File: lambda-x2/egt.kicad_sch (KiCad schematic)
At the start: 9 parts, among them U1 MAX31855KASA

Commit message: more progress
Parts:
- added C58, C60: 10nF 50V, Capacitor_SMD:C_0402_1005Metric, symbol Device:C
- added C59, C61, C62: 100n, Capacitor_SMD:C_0402_1005Metric, symbol Device:C
- added R92, R93: (no value), symbol Device:R
- added U15: (no value), symbol Sensor_Temperature:MAX31856
- C48, C50: value (none) -> 10nF 50V; footprint (none) -> Capacitor_SMD:C_0402_1005Metric
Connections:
- net GND: now also C58.2, C60.2, C61.2, C62.2, U15.1 (AGND), U15.14 (DGND)
- net SPI_CS: now also U15.9 (~{CS})
- net SPI_SCK: now also U15.10 (SCK)
- net SPI_SO: now also U15.11 (SDO)
- net Vcc: now also C61.1, C62.1, U15.5 (AVDD), U15.8 (DVDD)
- net at C49.2, C50.1, D7.1 (K)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: now also R92.1
- net at C48.1, C49.1, D7.2 (K)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: now also R93.1, U15.2 (BIAS)
- new net: C58.1, C59.1, R93.2, U15.3 (T-)
- new net: C59.2, C60.1, R92.2, U15.4 (T+)
- new net SPI_SI: U15.12 (SDI)
- no-connect marks 0 -> 2
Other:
- note added: "Optional part: 10x time more expensive more features protected up to 45V on inputs"
- moved on the sheet: C37, C43, D7, L1, L3

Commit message: Progress
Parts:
- R92, R93: value (none) -> 100R; footprint (none) -> Resistor_SMD:R_0402_1005Metric
- U15: value (none) -> MAX31856; footprint (none) -> Package_SO:TSSOP-14_4.4x5mm_P0.65mm
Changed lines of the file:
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@@
     (in_bom yes) (on_board yes)
     (property "Reference" "R92" (id 0) (at 44.45 96.52 90))
-    (property "Value" "" (id 1) (at 44.45 99.06 90))
-    (property "Footprint" "" (id 2) (at 44.45 99.822 90)
+    (property "Value" "100R" (id 1) (at 44.45 99.06 90))
+    (property "Footprint" "Resistor_SMD:R_0402_1005Metric" (id 2) (at 44.45 99.822 90)
       (effects (font (size 1.27 1.27)) hide)
     )
@@
     (in_bom yes) (on_board yes)
     (property "Reference" "R93" (id 0) (at 44.45 106.68 90))
-    (property "Value" "" (id 1) (at 44.45 109.22 90))
-    (property "Footprint" "" (id 2) (at 44.45 102.362 90)
+    (property "Value" "100R" (id 1) (at 44.45 109.22 90))
+    (property "Footprint" "Resistor_SMD:R_0402_1005Metric" (id 2) (at 44.45 102.362 90)
       (effects (font (size 1.27 1.27)) hide)
     )
@@
       (effects (font (size 1.27 1.27)) (justify left))
     )
-    (property "Value" "" (id 1) (at 83.2994 88.9 0)
-      (effects (font (size 1.27 1.27)) (justify left))
-    )
-    (property "Footprint" "" (id 2) (at 82.55 118.11 0)
+    (property "Value" "MAX31856" (id 1) (at 83.2994 88.9 0)
+      (effects (font (size 1.27 1.27)) (justify left))
+    )
+    (property "Footprint" "Package_SO:TSSOP-14_4.4x5mm_P0.65mm" (id 2) (at 82.55 118.11 0)
       (effects (font (size 1.27 1.27)) (justify left) hide)
     )

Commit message: Progress
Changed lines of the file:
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@@
+    (stroke (width 0) (type default) (color 0 0 0 0))
+  )
+  (wire (pts (xy 33.02 121.92) (xy 33.02 120.65))
     (stroke (width 0) (type default) (color 0 0 0 0))
   )
@@
     (stroke (width 0) (type default) (color 0 0 0 0))
   )
-  (wire (pts (xy 63.5 116.84) (xy 63.5 119.38))
+  (wire (pts (xy 63.5 116.84) (xy 63.5 121.92))
     (stroke (width 0) (type default) (color 0 0 0 0))
   )
@@
     (stroke (width 0) (type default) (color 0 0 0 0))
   )
-  (wire (pts (xy 52.07 116.84) (xy 52.07 119.38))
+  (wire (pts (xy 52.07 116.84) (xy 52.07 121.92))
     (stroke (width 0) (type default) (color 0 0 0 0))
   )
@@
     (pin "2")
   )
-  (symbol (lib_id "power:GND") (at 106.68 85.09 0) (unit 1)
+  (symbol (lib_name "GND_1") (lib_id "power:GND") (at 106.68 85.09 0) (unit 1)
     (in_bom yes) (on_board yes)
     (property "Reference" "#PWR0173" (id 0) (at 106.68 91.44 0)
       (effects (font (size 1.27 1.27)) hide)
     )
-    (property "Value" "GND" (id 1) (at 106.807 89.4842 0))
+    (property "Value" "" (id 1) (at 106.807 89.4842 0)
+      (effects (font (size 1.27 1.27)) hide)
+    )
     (property "Footprint" "" (id 2) (at 106.68 85.09 0)
       (effects (font (size 1.27 1.27)) hide)
@@
     (pin "2")
   )
-  (symbol (lib_id "power:GND") (at 90.17 29.21 0) (unit 1)
+  (symbol (lib_name "GND_4") (lib_id "power:GND") (at 90.17 29.21 0) (unit 1)
     (in_bom yes) (on_board yes)
     (property "Reference" "#PWR0150" (id 0) (at 90.17 35.56 0)
       (effects (font (size 1.27 1.27)) hide)
     )
-    (property "Value" "GND" (id 1) (at 90.297 33.6042 0))
+    (property "Value" "" (id 1) (at 90.297 33.6042 0)
+      (effects (font (size 1.27 1.27)) hide)
+    )
     (property "Footprint" "" (id 2) (at 90.17 29.21 0)
       (effects (font (size 1.27 1.27)) hide)
@@
     (pin "2")
   )
-  (symbol (lib_id "power:GND") (at 52.07 119.38 0) (unit 1)
-    (in_bom yes) (on_board yes)
-    (property "Reference" "#PWR0172" (id 0) (at 52.07 125.73 0)
-      (effects (font (size 1.27 1.27)) hide)
-    )
-    (property "Value" "GND" (id 1) (at 52.197 123.7742 0))
-    (property "Footprint" "" (id 2) (at 52.07 119.38 0)
-      (effects (font (size 1.27 1.27)) hide)
-    )
-    (property "Datasheet" "" (id 3) (at 52.07 119.38 0)
-      (effects (font (size 1.27 1.27)) hide)
-    )
-    (pin "1")
-  )
-  (symbol (lib_id "power:GND") (at 76.2 121.92 0) (unit 1)
+  (symbol (lib_name "GND_8") (lib_id "power:GND") (at 52.07 121.92 0) (unit 1)
+    (in_bom yes) (on_board yes)
+    (property "Reference" "#PWR0172" (id 0) (at 52.07 128.27 0)
+      (effects (font (size 1.27 1.27)) hide)
+    )
+    (property "Value" "" (id 1) (at 52.197 126.3142 0)
+      (effects (font (size 1.27 1.27)) hide)
+    )
+    (property "Footprint" "" (id 2) (at 52.07 121.92 0)
+      (effects (font (size 1.27 1.27)) hide)
+    )
+    (property "Datasheet" "" (id 3) (at 52.07 121.92 0)
+      (effects (font (size 1.27 1.27)) hide)
+    )
+    (pin "1")
+  )
+  (symbol (lib_name "GND_10") (lib_id "power:GND") (at 76.2 121.92 0) (unit 1)
     (in_bom yes) (on_board yes)
     (property "Reference" "#PWR0175" (id 0) (at 76.2 128.27 0)
       (effects (font (size 1.27 1.27)) hide)
     )
-    (property "Value" "GND" (id 1) (at 76.327 126.3142 0))
+    (property "Value" "" (id 1) (at 76.327 126.3142 0)
+      (effects (font (size 1.27 1.27)) hide)
+    )
     (property "Footprint" "" (id 2) (at 76.2 121.92 0)
       (effects (font (size 1.27 1.27)) hide)
@@
     (pin "1")
   )
-  (symbol (lib_id "power:GND") (at 81.28 121.92 0) (unit 1)
+  (symbol (lib_name "GND_11") (lib_id "power:GND") (at 81.28 121.92 0) (unit 1)
     (in_bom yes) (on_board yes)
     (property "Reference" "#PWR0176" (id 0) (at 81.28 128.27 0)
       (effects (font (size 1.27 1.27)) hide)
     )
-    (property "Value" "GND" (id 1) (at 81.407 126.3142 0))
+    (property "Value" "" (id 1) (at 81.407 126.3142 0)
+      (effects (font (size 1.27 1.27)) hide)
+    )
     (property "Footprint" "" (id 2) (at 81.28 121.92 0)
       (effects (font (size 1.27 1.27)) hide)
@@
     (pin "9")
   )
-  (symbol (lib_id "power:GND") (at 128.27 29.21 0) (unit 1)
+  (symbol (lib_name "GND_3") (lib_id "power:GND") (at 128.27 29.21 0) (unit 1)
     (in_bom yes) (on_board yes)
     (property "Reference" "#PWR0149" (id 0) (at 128.27 35.56 0)
       (effects (font (size 1.27 1.27)) hide)
     )
-    (property "Value" "GND" (id 1) (at 128.397 33.6042 0))
+    (property "Value" "" (id 1) (at 128.397 33.6042 0)
+      (effects (font (size 1.27 1.27)) hide)
+    )
     (property "Footprint" "" (id 2) (at 128.27 29.21 0)
       (effects (font (size 1.27 1.27)) hide)
@@
     (pin "1")
   )
-  (symbol (lib_id "power:GND") (at 53.34 59.69 0) (unit 1)
+  (symbol (lib_name "GND_5") (lib_id "power:GND") (at 53.34 59.69 0) (unit 1)
     (in_bom yes) (on_board yes)
     (property "Reference" "#PWR0156" (id 0) (at 53.34 66.04 0)
       (effects (font (size 1.27 1.27)) hide)
     )
-    (property "Value" "GND" (id 1) (at 53.467 64.0842 0))
+    (property "Value" "" (id 1) (at 53.467 64.0842 0)
+      (effects (font (size 1.27 1.27)) hide)
+    )
     (property "Footprint" "" (id 2) (at 53.34 59.69 0)
       (effects (font (size 1.27 1.27)) hide)
@@
     (pin "1")
   )
-  (symbol (lib_id "power:GND") (at 66.04 59.69 0) (unit 1)
+  (symbol (lib_name "GND_6") (lib_id "power:GND") (at 66.04 59.69 0) (unit 1)
     (in_bom yes) (on_board yes)
     (property "Reference" "#PWR0157" (id 0) (at 66.04 66.04 0)
       (effects (font (size 1.27 1.27)) hide)
     )
-    (property "Value" "GND" (id 1) (at 66.167 64.0842 0))
+    (property "Value" "" (id 1) (at 66.167 64.0842 0)
+      (effects (font (size 1.27 1.27)) hide)
+    )
     (property "Footprint" "" (id 2) (at 66.04 59.69 0)
       (effects (font (size 1.27 1.27)) hide)
@@
     (pin "1")
   )
-  (symbol (lib_id "power:GND") (at 80.01 57.15 0) (unit 1)
+  (symbol (lib_name "GND_7") (lib_id "power:GND") (at 80.01 57.15 0) (unit 1)
     (in_bom yes) (on_board yes)
     (property "Reference" "#PWR0148" (id 0) (at 80.01 63.5 0)
       (effects (font (size 1.27 1.27)) hide)
     )
-    (property "Value" "GND" (id 1) (at 80.137 61.5442 0))
+    (property "Value" "" (id 1) (at 80.137 61.5442 0)
+      (effects (font (size 1.27 1.27)) hide)
+    )
     (property "Footprint" "" (id 2) (at 80.01 57.15 0)
       (effects (font (size 1.27 1.27)) hide)
@@
     (pin "2")
   )
-  (symbol (lib_id "power:GND") (at 116.84 85.09 0) (unit 1)
+  (symbol (lib_name "GND_2") (lib_id "power:GND") (at 116.84 85.09 0) (unit 1)
     (in_bom yes) (on_board yes)
     (property "Reference" "#PWR0174" (id 0) (at 116.84 91.44 0)
       (effects (font (size 1.27 1.27)) hide)
     )
-    (property "Value" "GND" (id 1) (at 116.967 89.4842 0))
+    (property "Value" "" (id 1) (at 116.967 89.4842 0)
+      (effects (font (size 1.27 1.27)) hide)
+    )
     (property "Footprint" "" (id 2) (at 116.84 85.09 0)
       (effects (font (size 1.27 1.27)) hide)
@@
     (pin "2")
   )
-  (symbol (lib_id "power:GND") (at 63.5 119.38 0) (unit 1)
-    (in_bom yes) (on_board yes)
-    (property "Reference" "#PWR0177" (id 0) (at 63.5 125.73 0)
-      (effects (font (size 1.27 1.27)) hide)
-    )
-    (property "Value" "GND" (id 1) (at 63.627 123.7742 0))
-    (property "Footprint" "" (id 2) (at 63.5 119.38 0)
-      (effects (font (size 1.27 1.27)) hide)
-    )
-    (property "Datasheet" "" (id 3) (at 63.5 119.38 0)
-      (effects (font (size 1.27 1.27)) hide)
-    )
-    (pin "1")
-  )
-  (symbol (lib_id "power:GND") (at 33.02 120.65 0) (unit 1)
-    (in_bom yes) (on_board yes)
-    (property "Reference" "#PWR0154" (id 0) (at 33.02 127 0)
-      (effects (font (size 1.27 1.27)) hide)
-    )
-    (property "Value" "GND" (id 1) (at 33.147 125.0442 0))
-    (property "Footprint" "" (id 2) (at 33.02 120.65 0)
-      (effects (font (size 1.27 1.27)) hide)
-    )
-    (property "Datasheet" "" (id 3) (at 33.02 120.65 0)
-      (effects (font (size 1.27 1.27)) hide)
-    )
+  (symbol (lib_name "GND_9") (lib_id "power:GND") (at 63.5 121.92 0) (unit 1)
+    (in_bom yes) (on_board yes)
+    (property "Reference" "#PWR0177" (id 0) (at 63.5 128.27 0)
+      (effects (font (size 1.27 1.27)) hide)
+    )
+    (property "Value" "" (id 1) (at 63.627 126.3142 0)
+      (effects (font (size 1.27 1.27)) hide)
+    )
+    (property "Footprint" "" (id 2) (at 63.5 121.92 0)
+      (effects (font (size 1.27 1.27)) hide)
+    )
+    (property "Datasheet" "" (id 3) (at 63.5 121.92 0)
+      (effects (font (size 1.27 1.27)) hide)
+    )
+    (pin "1")
+  )
+  (symbol (lib_id "power:GND") (at 33.02 121.92 0) (unit 1)
+    (in_bom yes) (on_board yes)
+    (property "Reference" "#PWR0154" (id 0) (at 33.02 128.27 0)
+      (effects (font (size 1.27 1.27)) hide)
+    )
+    (property "Value" "" (id 1) (at 33.147 126.3142 0)
+      (effects (font (size 1.27 1.27)) hide)
+    )
+    (property "Footprint" "" (id 2) (at 33.02 121.92 0)
+      (effects (font (size 1.27 1.27)) hide)
+    )
+    (property "Datasheet" "" (id 3) (at 33.02 121.92 0)
+      (effects (font (size 1.27 1.27)) hide)
+    )

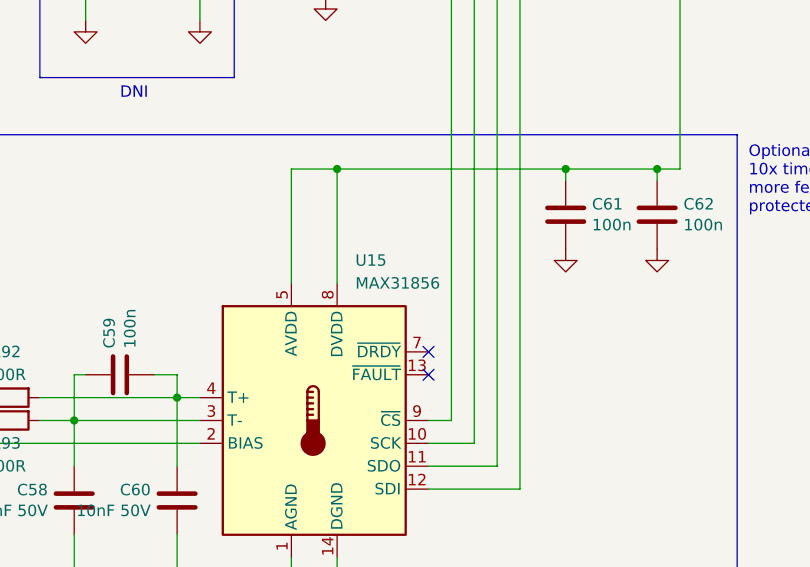
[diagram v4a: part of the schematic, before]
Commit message: Remove MAX31856 from BOM
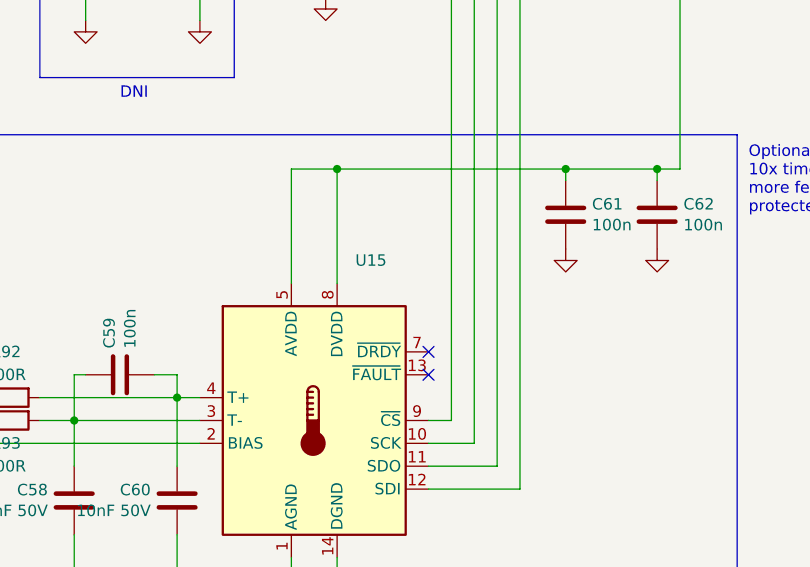
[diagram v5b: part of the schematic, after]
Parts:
- U15: value MAX31856 -> (none); footprint Package_SO:TSSOP-14_4.4x5mm_P0.65mm -> (none); now left out of the parts list
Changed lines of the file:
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@@
   )
   (symbol (lib_id "Sensor_Temperature:MAX31856") (at 78.74 104.14 0) (unit 1)
-    (in_bom yes) (on_board yes) (fields_autoplaced)
+    (in_bom no) (on_board yes) (fields_autoplaced)
     (property "Reference" "U15" (id 0) (at 83.2994 86.36 0)
       (effects (font (size 1.27 1.27)) (justify left))
     )
-    (property "Value" "MAX31856" (id 1) (at 83.2994 88.9 0)
+    (property "Value" "" (id 1) (at 83.2994 88.9 0)
       (effects (font (size 1.27 1.27)) (justify left))
     )
-    (property "Footprint" "Package_SO:TSSOP-14_4.4x5mm_P0.65mm" (id 2) (at 82.55 118.11 0)
+    (property "Footprint" "" (id 2) (at 82.55 118.11 0)
       (effects (font (size 1.27 1.27)) (justify left) hide)
     )

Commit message: lambda-x2: revork aux outputs, remove useless protection in LSU
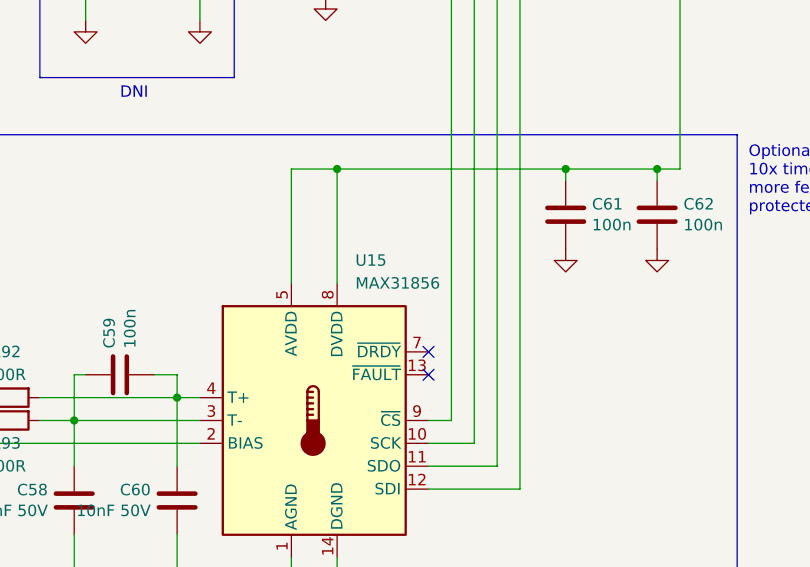
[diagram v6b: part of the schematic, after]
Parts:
- U15: value (none) -> MAX31856; footprint (none) -> Package_SO:TSSOP-14_4.4x5mm_P0.65mm
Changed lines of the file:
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@@
       (effects (font (size 1.27 1.27)) (justify left))
     )
-    (property "Value" "" (id 1) (at 83.2994 88.9 0)
+    (property "Value" "MAX31856" (id 1) (at 83.2994 88.9 0)
       (effects (font (size 1.27 1.27)) (justify left))
     )
-    (property "Footprint" "" (id 2) (at 82.55 118.11 0)
+    (property "Footprint" "Package_SO:TSSOP-14_4.4x5mm_P0.65mm" (id 2) (at 82.55 118.11 0)
       (effects (font (size 1.27 1.27)) (justify left) hide)
     )

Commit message: lambda-x2: final update, rev1
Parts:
- U1: value MAX31855KASA -> (none); footprint Package_SO:SOIC-8_3.9x4.9mm_P1.27mm -> (none); LCSC (none) -> C52028
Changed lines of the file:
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@@
       (effects (font (size 1.27 1.27)) (justify left))
     )
-    (property "Value" "MAX31855KASA" (id 1) (at 82.0294 34.29 0)
+    (property "Value" "" (id 1) (at 82.0294 34.29 0)
       (effects (font (size 1.27 1.27)) (justify left))
     )
-    (property "Footprint" "Package_SO:SOIC-8_3.9x4.9mm_P1.27mm" (id 2) (at 105.41 53.34 0)
+    (property "Footprint" "" (id 2) (at 105.41 53.34 0)
       (effects (font (size 1.27 1.27) italic) hide)
     )
@@
       (effects (font (size 1.27 1.27)) hide)
     )
+    (property "LCSC" "C52028" (id 4) (at 80.01 44.45 0)
+      (effects (font (size 1.27 1.27)) hide)
+    )

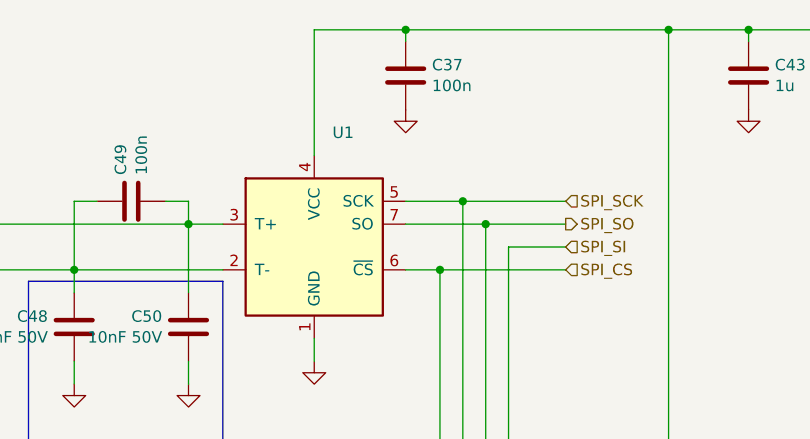
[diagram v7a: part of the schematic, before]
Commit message: lambda-x2: update BOM per JLC availability
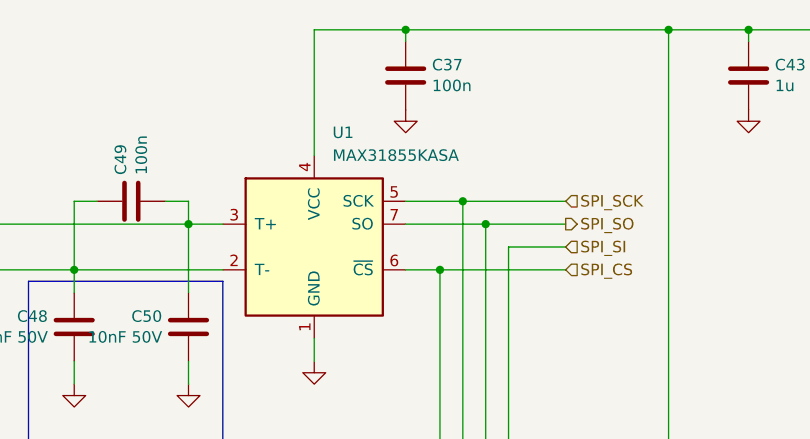
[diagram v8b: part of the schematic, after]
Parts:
- U1: value (none) -> MAX31855KASA; footprint (none) -> Package_SO:SOIC-8_3.9x4.9mm_P1.27mm
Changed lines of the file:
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@@
       (effects (font (size 1.27 1.27)) (justify left))
     )
-    (property "Value" "" (id 1) (at 82.0294 34.29 0)
+    (property "Value" "MAX31855KASA" (id 1) (at 82.0294 34.29 0)
       (effects (font (size 1.27 1.27)) (justify left))
     )
-    (property "Footprint" "" (id 2) (at 105.41 53.34 0)
+    (property "Footprint" "Package_SO:SOIC-8_3.9x4.9mm_P1.27mm" (id 2) (at 105.41 53.34 0)
       (effects (font (size 1.27 1.27) italic) hide)
     )
